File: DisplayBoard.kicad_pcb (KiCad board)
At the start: 4 copper layers, 35.6 x 38.1 mm, 32 parts, among them J301 Conn_01x12_Pin, J401 Conn_01x04, Q301 C42441446, U201 ESP32-S3-PICO-1-N8R2, U401 SN65HVD232, U501 AMS1117-3.3

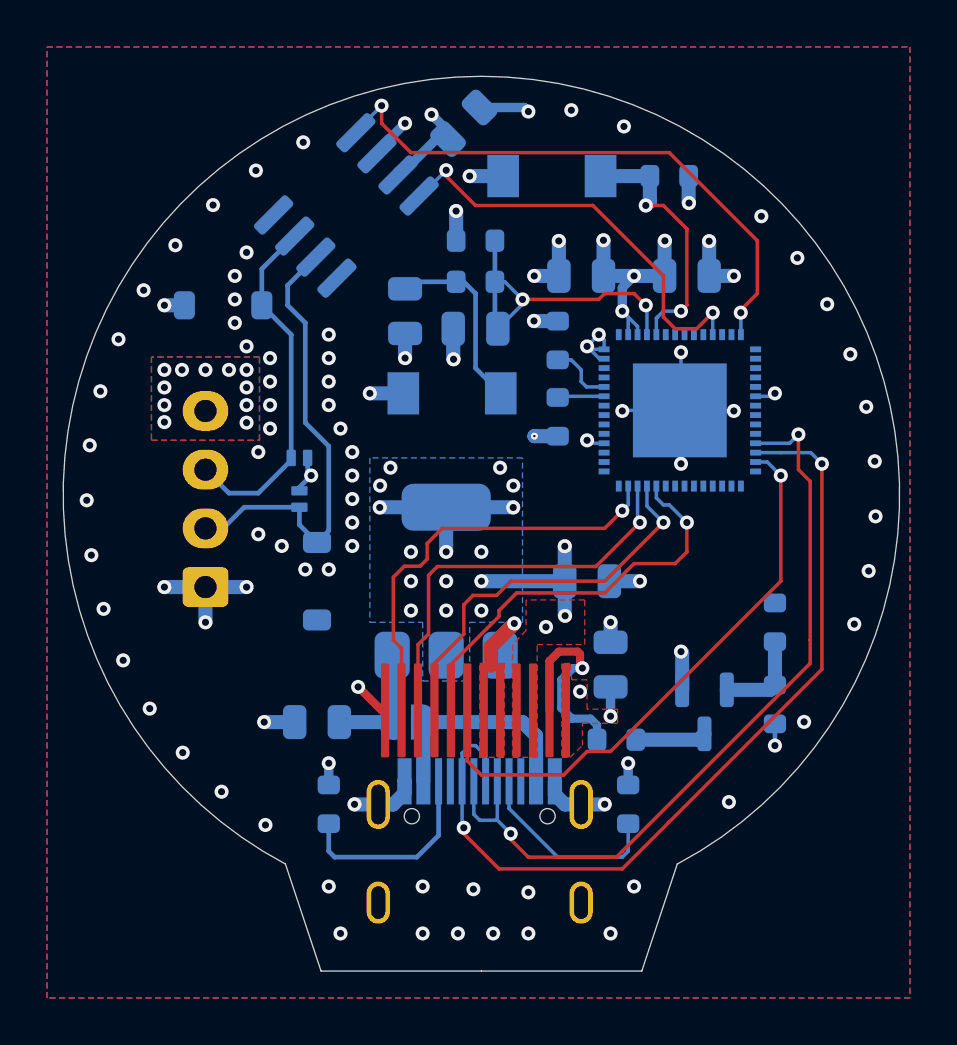
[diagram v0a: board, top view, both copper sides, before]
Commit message: Reworked DisplayBoard circuitry and layout; v1.1
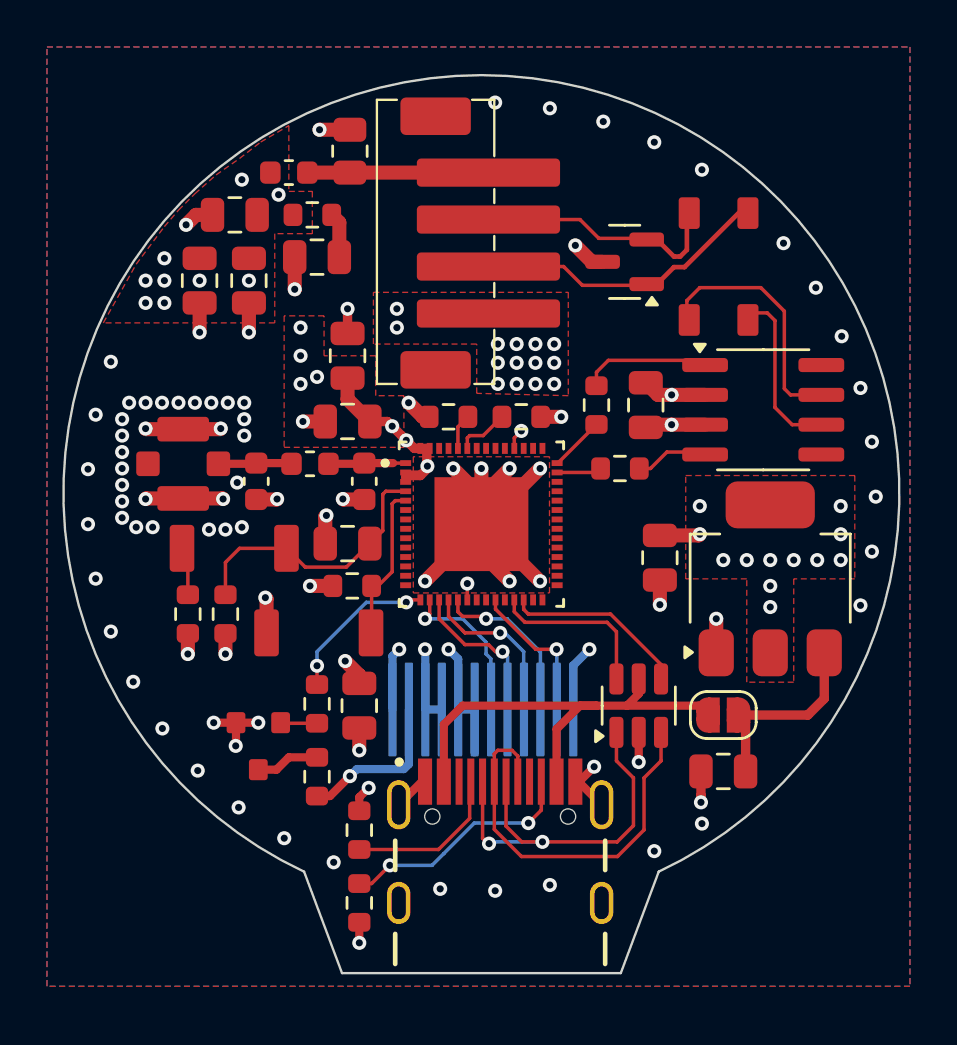
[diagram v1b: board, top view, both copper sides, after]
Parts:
- removed D403, D404: 3.3V, Diode_SMD:D_SOD-123
- removed R303: 10, Resistor_SMD:R_0603_1608Metric
- added C205: 3.3pF, Capacitor_SMD:C_0603_1608Metric, F.Cu at (95.0, 117.2)
- added C402: unkwn, Capacitor_SMD:C_0805_2012Metric, F.Cu at (88.0, 108.7)
- added C403: 100nF, Capacitor_SMD:C_0805_2012Metric, F.Cu at (89.5, 105.9)
- added C404: 47uF, Capacitor_SMD:C_0805_2012Metric, F.Cu at (93.0, 107.7)
- added C405: 100nF, Capacitor_SMD:C_0805_2012Metric, F.Cu at (107.0, 114.0)
- added FB401: BLM18KG121TN1D, Inductor_SMD:L_0603_1608Metric, F.Cu at (91.8, 104.1)
- added J201: Conn_Coaxial, CustomFootprints:CONMHF1-SMD-G-T_U.FL, F.Cu at (87.3, 116.5)
- added L201: 2.2nH, Inductor_SMD:L_0603_1608Metric, F.Cu at (92.7, 116.5)
- added L401: TDK ACT45B-510-2P-TL003, CustomFootprints:TDK ACT45B-510-2P-TL003, F.Cu at (110.1, 108.1)
- added R206: 10k, Resistor_SMD:R_0603_1608Metric, F.Cu at (98.6, 114.5)
- added R401: 3, Resistor_SMD:R_0603_1608Metric, F.Cu at (92.8, 105.9)
- added R402: 100, Resistor_SMD:R_0603_1608Metric, F.Cu at (105.9, 116.7)
- added U502: AMS1117-3.3, Package_TO_SOT_SMD:SOT-223-3_TabPin2, F.Cu at (112.3, 121.4)
- C201: value 0.1uF -> 1uF; moved to F.Cu
- C202: value C -> 22uF; moved to F.Cu
- C203: value 22uF -> 0.1uF; moved to F.Cu
- C204: value 0.1uF -> 3.3pF; footprint Capacitor_SMD:C_0805_2012Metric -> Capacitor_SMD:C_0603_1608Metric; moved to F.Cu
- C301, C501, C502, JP501, R202, R203, R205, Rusb501, Rusb502, U401, USBC501: moved to F.Cu
- C401: value 100nF -> unkwn; moved to F.Cu
- D401: value C502551 -> SP4020-01FTG-C; footprint Diode_SMD:D_SOD-882 -> Resistor_SMD:R_0805_2012Metric; moved to F.Cu
- D402: value V_C=12V V_B=3.6V V_RWM=3.3V -> PESD1CAN; footprint Diode_SMD:D_SOD-882 -> Package_TO_SOT_SMD:SOT-23; moved to F.Cu
- J301: footprint CustomFootprints:GC9A01-Connector -> CustomFootprints:GC9A01_Connector; moved to B.Cu
- J401: footprint Connector_JST:JST_XH_B4B-XH-A_1x04_P2.50mm_Vertical -> CustomFootprints:JST_PH_B4B_SM4_TB; moved to F.Cu
- Q301: value C42441446 -> L2N7002SLLT1G; footprint Package_TO_SOT_SMD:SOT-23 -> CustomFootprints:SOT_TO_92_L2N7002SLLT1G; moved to F.Cu
- R201: value 10k -> 470; moved to F.Cu
- R204: value 10k -> 100; moved to F.Cu
- R301: value 1K -> 1k; moved to F.Cu
- R302: value 10K -> 10; moved to F.Cu
- RST201, SPST201: footprint TS-1088-AR02016:SMD_Push_Button -> CustomFootprints:XUNPU_Button; moved to F.Cu
- U201: footprint ESP32-S3-PICO-1:PQFN40P700X700X106-57N -> CustomFootprints:ESP32-S3-PICO-1; moved to F.Cu
- U501: value AMS1117-3.3 -> USBLC6-2SC6; footprint Package_TO_SOT_SMD:SOT-223-3_TabPin2 -> Package_TO_SOT_SMD:SOT-23-6; moved to F.Cu
- moved SPST201 22.9 mm to (90.8, 123.7)
- moved R203 22.1 mm to (94.5, 121.7), turned to 180 degrees
- moved C204 20.3 mm to (90.4, 117.2), turned to -90 degrees
- moved R301 19.8 mm to (93.0, 126.7)
- moved U401 19.8 mm to (112.0, 114.2), turned to 0 degrees
- moved R302 19.7 mm to (93.0, 129.8), turned to -90 degrees
- moved R202 19.1 mm to (89.1, 122.9), turned to 90 degrees
- moved Q301 19.1 mm to (90.5, 128.5), turned to 0 degrees
- moved J401 18.7 mm to (99.9, 107.1), turned to -90 degrees
- moved R201 18.7 mm to (87.5, 122.9), turned to 90 degrees
- moved C501 17.4 mm to (110.3, 129.6)
- moved D402 17.1 mm to (106.1, 107.9), turned to 180 degrees
- moved JP501 13.5 mm to (110.3, 127.2), turned to 0 degrees
- moved RST201 13.3 mm to (87.2, 120.1)
- moved D401 13.2 mm to (94.4, 103.2), turned to 90 degrees
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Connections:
- net Net-(SPST201-B) renamed /MCU/BOOT
- net Net-(USBC501-CC1) renamed /USB/CC1
- net Net-(USBC501-CC2) renamed /USB/CC2
- C201 pad 1: Net-(RST201-B) -> /MCU/CHIP_PU
- C202 pad 1: Net-(U201-CHIP_PU) -> +3.3V
- C204 pad 1: +3.3V -> /MCU/ANTENNA
- C501 pad 1: Net-(JP501-B) -> /USB/5V_VBUS
- D401 pad 1: GND -> /CAN/UNF_3.3V
- D401 pad 2: CANH -> GND
- D402 pad 1: GND -> /CAN/UNF_CANN
- D402 pad 2: CANL -> /CAN/UNF_CANP
- J301 pad 10: /GC9A01/DIN -> /MCU/DIN
- J301 pad 11: /GC9A01/RST -> /MCU/RST
- J301 pad 7: /GC9A01/DC -> /MCU/DC
- J301 pad 8: /GC9A01/CS -> /MCU/CS
- J301 pad 9: /GC9A01/CLK -> /MCU/CLK
- J401 pad 1: GND -> /CAN/UNF_3.3V
- J401 pad 2: CANL -> /CAN/UNF_CANP
- J401 pad 3: CANH -> /CAN/UNF_CANN
- J401 pad 4: +3.3V -> GND
- JP501 pad 1: Net-(JP501-A) -> VBUS
- JP501 pad 2: Net-(JP501-B) -> /USB/5V_VBUS
- Q301 pad 1: GND -> /GC9A01/LIM_BL
- Q301 pad 2: Net-(Q301-B) -> GND
- Q301 pad 3: Net-(Q301-C) -> /GC9A01/GUI_LIM_LEDK
- R201 pad 1: Net-(RST201-B) -> GND
- R201 pad 2: Net-(U201-CHIP_PU) -> Net-(RST201-A)
- R202 pad 2: Net-(U201-CHIP_PU) -> /MCU/CHIP_PU
- R204 pad 1: GND -> Net-(U201-GPIO37)
- R204 pad 2: Net-(U201-GPIO45) -> /CAN/CAN_TX
- R205 pad 2: Net-(U201-GPIO46) -> /MCU/VDD_SPI
- R301 pad 1: BL -> /MCU/BL
- R301 pad 2: Net-(Q301-B) -> /GC9A01/LIM_BL
- R302 pad 1: +3.3V -> /GC9A01/GUI_LIM_LEDK
- R302 pad 2: Net-(Q301-B) -> LEDK
- RST201 pad 1: GND -> Net-(RST201-A)
- RST201 pad 2: Net-(RST201-B) -> /MCU/CHIP_PU
- U201 pad 1: unconnected-(U201-LNA_IN-Pad1) -> LDA_IN
- U201 pad 11: /CAN/CAN_RX -> unconnected-(U201-GPIO6-Pad11)
- U201 pad 14: /CAN/CAN_TX -> unconnected-(U201-GPIO9-Pad14)
- U201 pad 15: unconnected-(U201-GPIO10-Pad15) -> /MCU/BL
- U201 pad 16: unconnected-(U201-GPIO11-Pad16) -> /MCU/DC
- U201 pad 17: unconnected-(U201-GPIO12-Pad17) -> /MCU/CS
- U201 pad 18: unconnected-(U201-GPIO13-Pad18) -> /MCU/CLK
- U201 pad 19: unconnected-(U201-GPIO14-Pad19) -> /MCU/DIN
- U201 pad 23: unconnected-(U201-GPIO17-Pad23) -> /MCU/RST
- U201 pad 27: /GC9A01/DC -> unconnected-(U201-GPIO21-Pad27)
- U201 pad 38: /GC9A01/CS -> unconnected-(U201-GPIO33-Pad38)
- U201 pad 39: /GC9A01/CLK -> unconnected-(U201-GPIO34-Pad39)
- U201 pad 4: Net-(U201-CHIP_PU) -> /MCU/CHIP_PU
- U201 pad 40: /GC9A01/DIN -> unconnected-(U201-GPIO35-Pad40)
- U201 pad 41: /GC9A01/RST -> /CAN/CAN_RX
- U201 pad 42: unconnected-(U201-GPIO37-Pad42) -> Net-(U201-GPIO37)
- U201 pad 51: Net-(U201-GPIO45) -> /MCU/VDD_SPI
- U201 pad 52: Net-(U201-GPIO46) -> /MCU/ROM_PRINT
- U401 pad 4: /CAN/CAN_RX -> Net-(U401-R)
- U501 pad 1: GND -> UNF_USB_D-
- U501 pad 2: +3.3V -> GND
- U501 pad 3: Net-(JP501-B) -> UNF_USB_D+
- USBC501 pad A4_B9: Net-(JP501-A) -> VBUS
- USBC501 pad A6: /MCU/USB_D+ -> UNF_USB_D+
- USBC501 pad A7: /MCU/USB_D- -> UNF_USB_D-
- USBC501 pad B4_A9: Net-(JP501-A) -> VBUS
- USBC501 pad B6: /MCU/USB_D+ -> UNF_USB_D+
- USBC501 pad B7: /MCU/USB_D- -> UNF_USB_D-
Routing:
- net /MCU/USB_D+: track 37.0 -> 7.84 mm, vias 2 -> 0
- net /MCU/USB_D-: track 33.6 -> 7.22 mm, vias 2 -> 0
- net GND: track 51.8 -> 78.1 mm, vias 96 -> 108
- net /GC9A01/DC: track 25.0 -> 0.00 mm, vias 1 -> 0
- net VBUS: track 0.00 -> 19.9 mm
- net /CAN/CAN_TX: track 24.7 -> 5.42 mm, vias 2 -> 0
- net /GC9A01/RST: track 18.3 -> 0.00 mm, vias 1 -> 0
- net /GC9A01/CS: track 17.6 -> 0.00 mm, vias 1 -> 0
- net /GC9A01/DIN: track 17.5 -> 0.00 mm, vias 1 -> 0
- net UNF_USB_D-: track 0.00 -> 17.3 mm, vias 0 -> 2
- net +3.3V: track 37.0 -> 19.8 mm, vias 42 -> 35
- net UNF_USB_D+: track 0.00 -> 17.2 mm
- net /GC9A01/CLK: track 16.8 -> 0.00 mm, vias 1 -> 0
- net /CAN/CAN_RX: track 18.1 -> 1.92 mm, vias 2 -> 0
- net Net-(U201-CHIP_PU): track 13.8 -> 0.00 mm, vias 2 -> 0
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- removed copper zone on B.Cu, net +3.3V
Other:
- board size 35.6 x 38.1 mm -> 35.6 x 38.2 mm
- board text added: "MX5-HybridDash"
- board text added: "Made by VogelPapaFinn & Streetlamp"
- board text added: "v1.1"
